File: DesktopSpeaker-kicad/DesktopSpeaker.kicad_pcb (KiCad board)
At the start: 4 copper layers, 116 x 112 mm, 315 parts, among them J1 USB_C_Receptacle_USB2.0_16P, J10 B2P-VH, J11 B2P-VH, J2 HEAD_OUT, J3 AUX_IN, J4 I2C service, J5 1S_PACK_3PIN, J6 SWD, J7 SWD_TC2030, J8 BM83_PROG, J9 B2P-VH, Q100 2N7002, Q101 2N7002, Q102 2N7002, Q103 CSD17579Q3A, Q104 2N7002, SW100 WAKE_QON, SW101 BAT_DISCONNECT, U1 BM83SM1-00TA, U10 TPA6132A2RTER, U11 TPS25730DREFR, U12 TPS7A0230PDBVR, U13 TS5A3167DBVR, U14 TPS63802DLAR, U15 TPS63802DLAR, U16 TS5A3167DBVR, U17 TS5A3167DBVR, U19 TPS7B8450QWDRBRQ1, U2 PCM2902CDBR, U20 TPS2116DRLR, U21 TPS3839G33DBZR, U22 TPS7A2033PDBVR, U23 TPS22917DBVR, U24 PCM1862DBTR, U25 TPS61088RHLR, U3 STM32G071RBT6, U4 BQ25792RQMR, U5 MAX17048G+T10, U6 TAS5825MRHBR, U7 TAS5825MRHBR, U8 TS5A23157DGSR, U9 TS5A23157DGSR, Y170 12MHz, Y200 24.576MHz

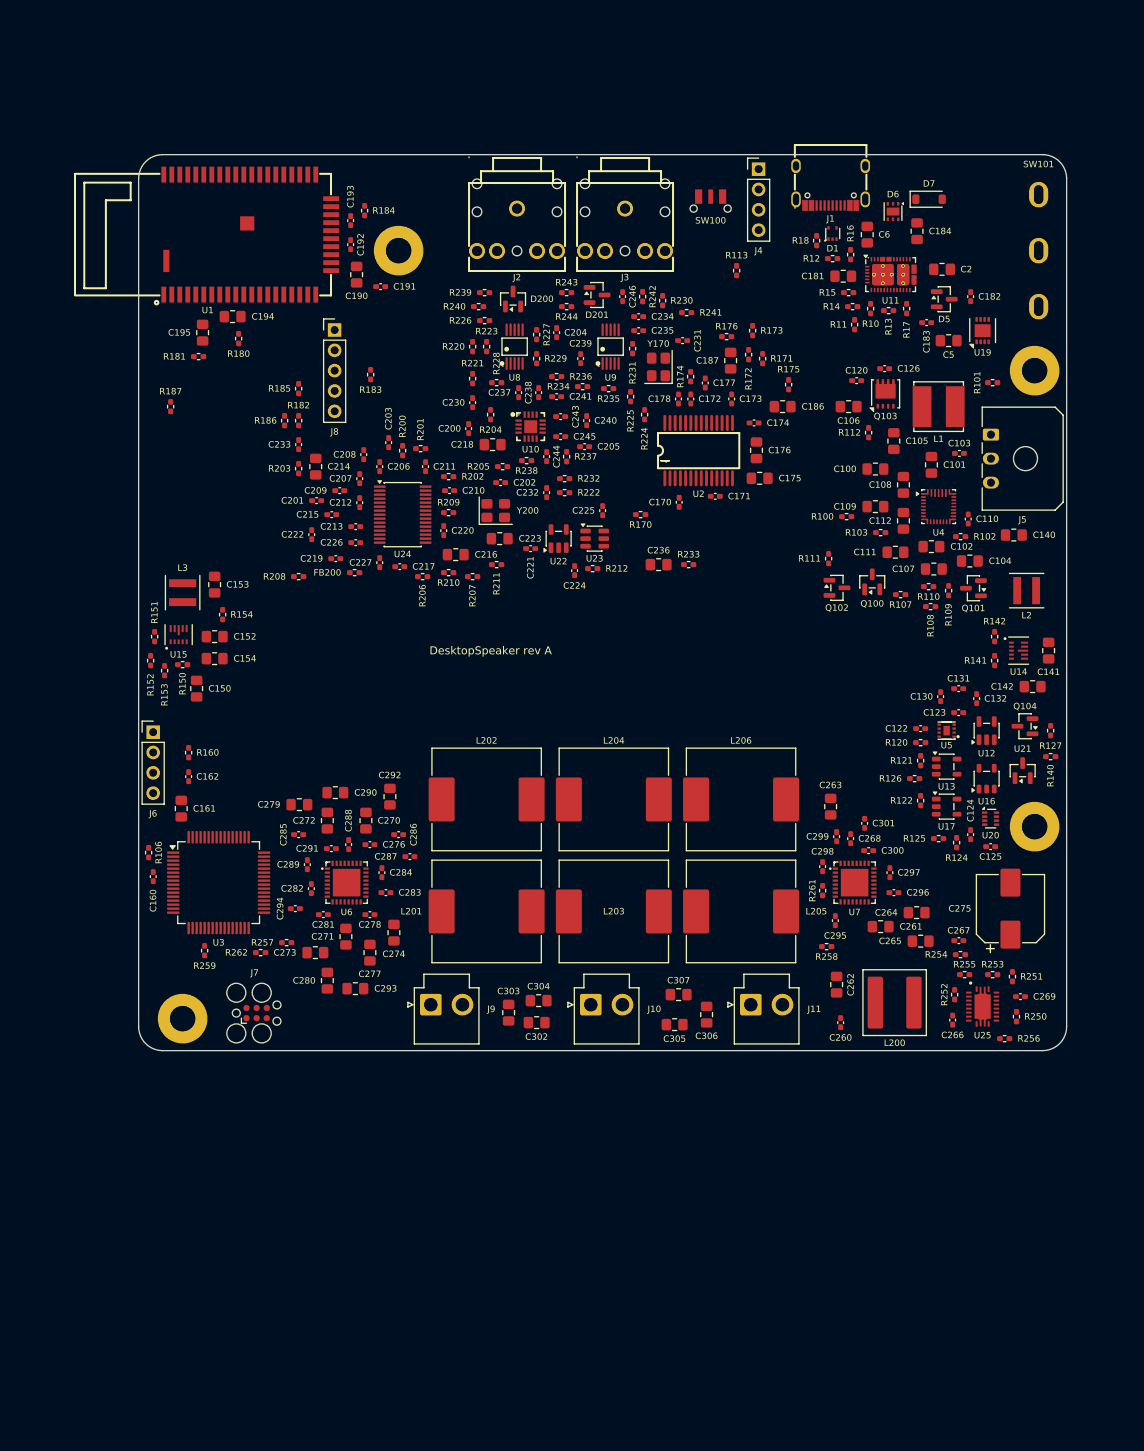
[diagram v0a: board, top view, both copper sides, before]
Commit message: WIP placement v4: tiled functional cells with section boxes (board larger than v3; compaction pending)
Co-Authored-By: Claude Sonnet 5.5 <noreply@anthropic.com>
Claude-Session: https://claude.ai/code/session_01N5RHheWSjDFDPbKVD5YVeJ
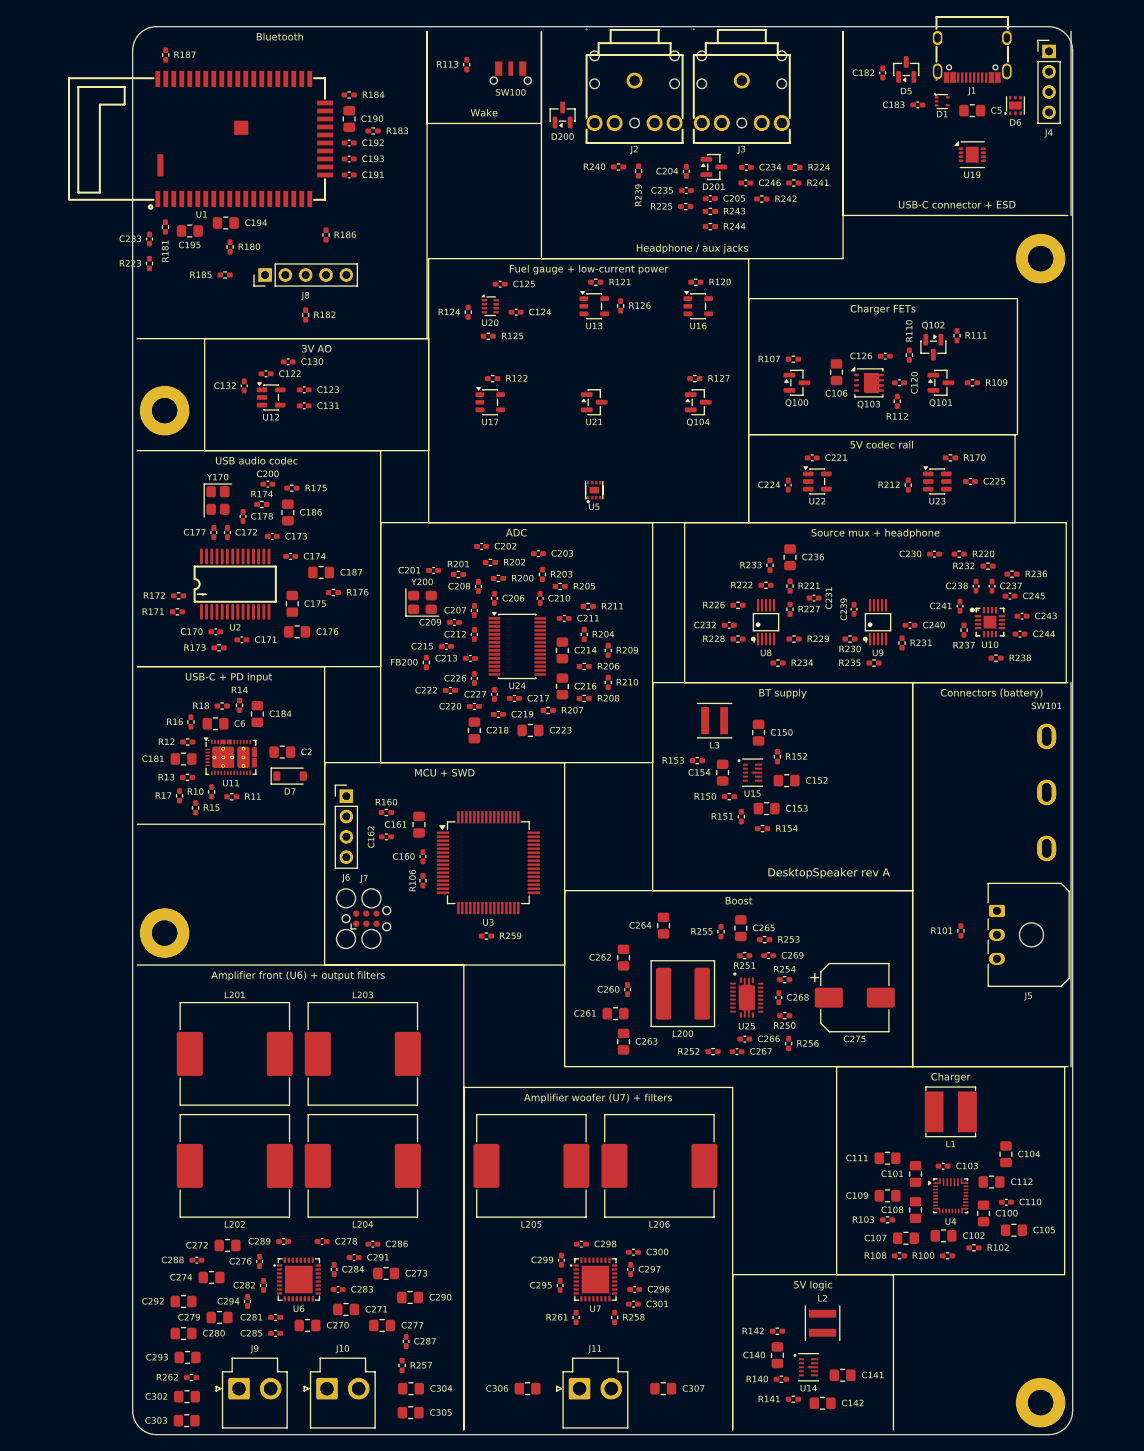
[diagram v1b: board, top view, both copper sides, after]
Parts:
- moved R17 109.4 mm to (97.1, 116.1), turned to 90 degrees
- moved H4 108.9 mm to (95.2, 68.0)
- moved D7 107.6 mm to (110.9, 113.7)
- moved C140 106.7 mm to (171.8, 186.1), turned to 90 degrees
- moved R13 105.3 mm to (98.1, 113.8)
- moved R15 104.0 mm to (99.1, 117.6), turned to 90 degrees
- moved C2 102.2 mm to (110.0, 110.7)
- moved C181 102.2 mm to (97.6, 111.5)
- moved C184 102.2 mm to (106.8, 105.9)
- moved U11 102.2 mm to (103.5, 111.3)
- moved R10 102.2 mm to (101.1, 115.6), turned to 90 degrees
- moved C6 101.9 mm to (101.6, 107.1), turned to 0 degrees
- moved R16 101.1 mm to (98.5, 106.9), turned to 90 degrees
- moved R12 100.7 mm to (98.1, 109.4)
- moved C105 99.8 mm to (201.4, 170.4), turned to 0 degrees
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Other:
- board size 116 x 112 mm -> 117.5 x 176 mm
- board text added: "3V AO"
- board text added: "5V codec rail"
- board text added: "5V logic"
- board text added: "ADC"
- board text added: "Amplifier front (U6) + output filters"
- board text added: "Amplifier woofer (U7) + filters"
- board text added: "BT supply"
- board text added: "Bluetooth"
- board text added: "Boost"
- board text added: "Charger"
- board text added: "Charger FETs"
- board text added: "Connectors (battery)"
- board text added: "Fuel gauge + low-current power"
- board text added: "Headphone / aux jacks"
- board text added: "MCU + SWD"
- board text added: "Source mux + headphone"
- board text added: "USB audio codec"
- board text added: "USB-C + PD input"
- board text added: "USB-C connector + ESD"
- board text added: "Wake"

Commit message: Placement v5: tiled functional cells at minimum separations, better decoupling, woofer chamber auto-sized; CAD rebuilt
Co-Authored-By: Claude Sonnet 5.5 <noreply@anthropic.com>
Claude-Session: https://claude.ai/code/session_01N5RHheWSjDFDPbKVD5YVeJ
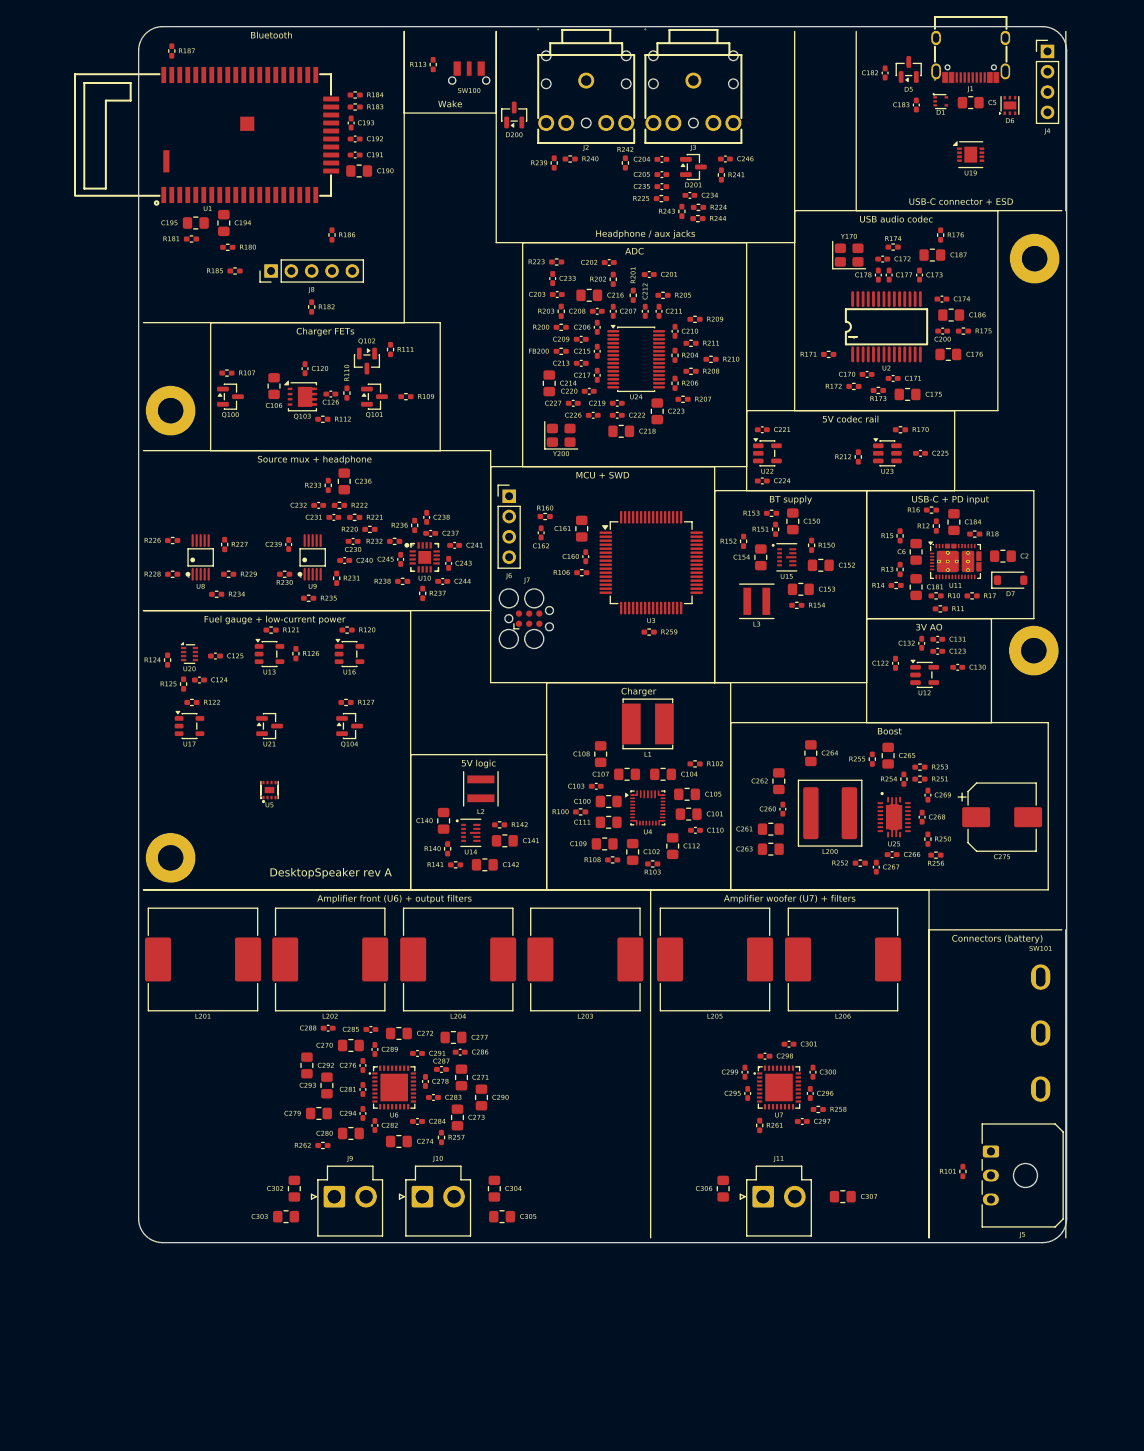
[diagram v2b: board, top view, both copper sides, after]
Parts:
- moved R17 102.2 mm to (196.2, 91.2), turned to 0 degrees
- moved R12 97.4 mm to (191.7, 82.4), turned to 90 degrees
- moved R18 96.5 mm to (196.5, 83.4)
- moved R16 96.3 mm to (191.1, 80.4), turned to 180 degrees
- moved R15 94.4 mm to (187.2, 83.7)
- moved C181 94.1 mm to (189.2, 90.1), turned to -90 degrees
- moved H2 94.0 mm to (203.9, 98.0)
- moved R10 93.8 mm to (191.7, 91.2), turned to 0 degrees
- moved U11 93.8 mm to (194.1, 86.9)
- moved D7 93.3 mm to (201.0, 89.2)
- moved C2 93.3 mm to (200.0, 86.2)
- moved R13 92.8 mm to (187.2, 87.9), turned to -90 degrees
- moved C130 92.0 mm to (194.4, 100.1)
- moved R11 91.6 mm to (192.2, 92.8)
- moved C132 90.6 mm to (189.9, 97.1)
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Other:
- board size 117.5 x 176 mm -> 116 x 152 mm

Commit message: Placement v6: shrink-wrapped tiles, 116x138 mm (area/depth targets unmet; decap snap pass pending)
Co-Authored-By: Claude Sonnet 5.5 <noreply@anthropic.com>
Claude-Session: https://claude.ai/code/session_01N5RHheWSjDFDPbKVD5YVeJ
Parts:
- moved H4 136.7 mm to (203.9, 152.0)
- moved H2 107.9 mm to (96.0, 97.0)
- moved SW101 91.6 mm to (204.8, 54.2)
- moved J5 91.6 mm to (198.5, 69.0)
- moved R101 91.6 mm to (195.0, 71.5)
- moved C262 74.6 mm to (97.5, 117.8), turned to 180 degrees
- moved C269 73.6 mm to (117.2, 112.5)
- moved R250 73.6 mm to (117.2, 118.0)
- moved R251 73.6 mm to (116.2, 110.5)
- moved R253 73.6 mm to (116.2, 109.0)
- moved R254 73.6 mm to (114.2, 110.5)
- moved R256 73.6 mm to (118.2, 120.0)
- moved C265 73.6 mm to (112.2, 107.6)
- moved C266 73.6 mm to (112.7, 120.0)
- moved C268 73.6 mm to (116.4, 115.3)
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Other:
- board size 116 x 152 mm -> 116 x 138 mm

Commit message: Decap snap: 0402 decoupling caps against supply pins, reference labels on F.Fab; min_text_height restore
Co-Authored-By: Claude Sonnet 5.5 <noreply@anthropic.com>
Claude-Session: https://claude.ai/code/session_01N5RHheWSjDFDPbKVD5YVeJ
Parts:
- moved R185 26.4 mm to (104.0, 22.4), turned to 180 degrees
- moved C263 19.5 mm to (116.6, 116.5), turned to 90 degrees
- moved R160 18.2 mm to (157.4, 85.8), turned to 180 degrees
- moved C261 17.8 mm to (114.2, 120.2), turned to 0 degrees
- moved R186 17.0 mm to (118.6, 27.3), turned to 0 degrees
- moved R233 16.7 mm to (133.3, 67.7), turned to 90 degrees
- moved C236 16.1 mm to (129.2, 67.4), turned to 180 degrees
- moved R182 15.9 mm to (118.6, 29.9), turned to 180 degrees
- moved C216 14.5 mm to (169.0, 59.1), turned to 180 degrees
- moved R108 13.2 mm to (174.9, 103.3), turned to 0 degrees
- moved C272 12.6 mm to (118.3, 141.8), turned to 90 degrees
- moved C260 11.8 mm to (110.1, 119.5)
- moved C288 11.6 mm to (124.5, 141.4), turned to 180 degrees
- moved C286 11.6 mm to (124.8, 142.7), turned to 0 degrees
- moved C304 11.2 mm to (132.5, 152.4), turned to 180 degrees
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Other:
- board text added: "Battery I/O"
- board text added: "Jacks"
- board text removed: "Connectors (battery)"
- board text removed: "Headphone / aux jacks"
